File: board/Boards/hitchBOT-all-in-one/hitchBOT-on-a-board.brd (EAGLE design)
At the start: 160 x 100 mm, 7 parts

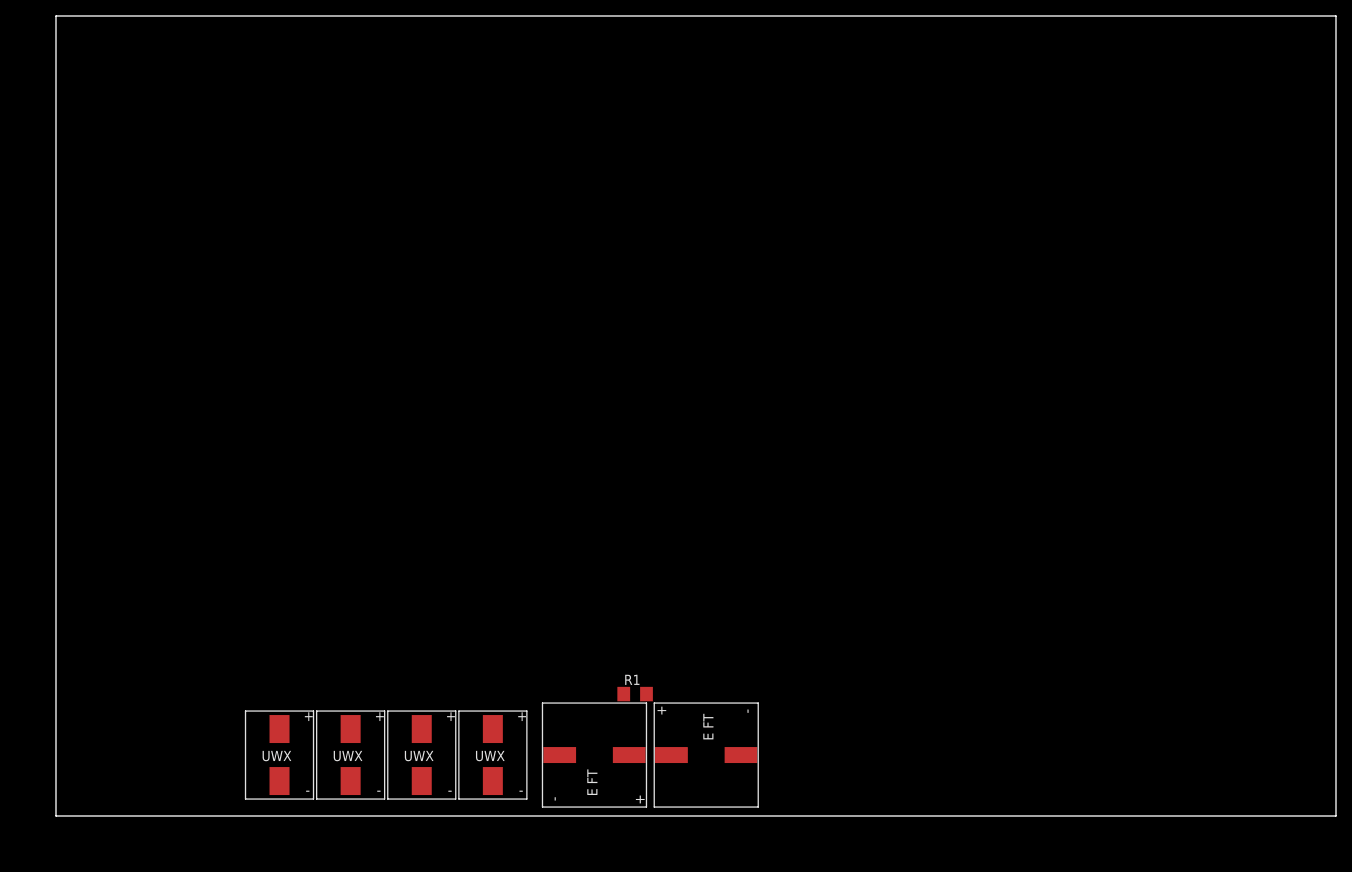
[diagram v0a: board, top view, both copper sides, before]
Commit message: updated board, now matches dimensions and layout of minibox board
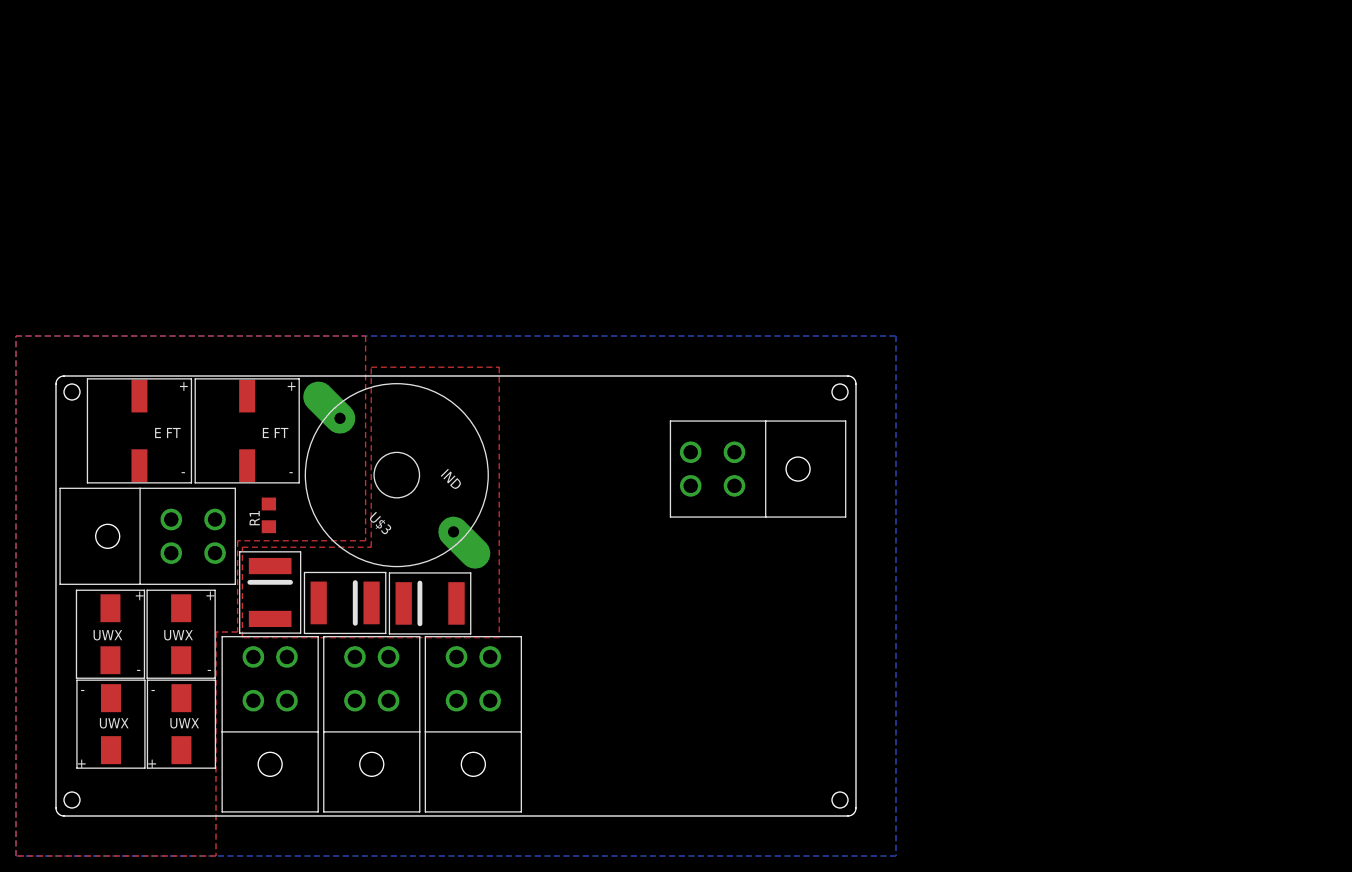
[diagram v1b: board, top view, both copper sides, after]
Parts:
- added U$10, U$11, U$4, U$5, U$6: 2X2-MOLEX, Molex:2X2MOLEX
- added U$3: INDUCTOR-M8365, macgrid:INDUCTOR-M8365
- added U$7, U$8, U$9: DO-214AB, macgrid:DO-214AB
- moved U$2 70.2 mm to (23.9, 48.1), turned to 0 degrees
- moved U$1 69.8 mm to (10.4, 48.1), turned to 0 degrees
- moved R1 50.9 mm to (26.6, 37.6), turned to 90 degrees
- moved C1 50.1 mm to (6.81, 22.7)
- moved C2 30.3 mm to (15.7, 11.5), turned to 180 degrees
- moved C4 30.2 mm to (6.87, 11.5), turned to 180 degrees
- moved C3 19.5 mm to (15.6, 22.7)
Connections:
- new net N$3: U$5.POWERL, U$5.POWERR, U$7.IN
- new net N$4: U$6.POWERL, U$6.POWERR, U$8.IN
- new net N$5: U$4.POWERL, U$4.POWERR, U$9.IN
- new net N$6: U$3.P$1, U$7.OUT, U$8.OUT, U$9.OUT
- net GND: now also U$10.GNDL, U$10.GNDR, U$11.GNDL, U$11.GNDR, U$4.GNDL, U$4.GNDR, U$5.GNDL, U$5.GNDR, U$6.GNDL, U$6.GNDR
- net N$1: now also U$10.POWERL, U$10.POWERR, U$3.P$2
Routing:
- added copper zone on layer 16, net GND
- added copper zone on layer 1, net N$1
- added copper zone on layer 1, net N$6
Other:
- board size 160 x 100 mm -> 100 x 55 mm
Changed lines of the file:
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@@
 <setting verticaltext="up"/>
 </settings>
-<grid distance="0.05" unitdist="inch" unit="inch" style="lines" multiple="1" display="no" altdistance="0.025" altunitdist="inch" altunit="inch"/>
+<grid distance="0.1" unitdist="mm" unit="mm" style="lines" multiple="1" display="no" altdistance="0.5" altunitdist="mm" altunit="mm"/>
 <layers>
 <layer number="1" name="Top" color="4" fill="1" visible="yes" active="yes"/>
@@
 <layer number="43" name="vRestrict" color="2" fill="10" visible="yes" active="yes"/>
 <layer number="44" name="Drills" color="7" fill="1" visible="no" active="yes"/>
-<layer number="45" name="Holes" color="7" fill="1" visible="no" active="yes"/>
+<layer number="45" name="Holes" color="7" fill="1" visible="yes" active="yes"/>
 <layer number="46" name="Milling" color="3" fill="1" visible="no" active="yes"/>
 <layer number="47" name="Measures" color="7" fill="1" visible="no" active="yes"/>
@@
 <board>
 <plain>
-<wire x1="0" y1="0" x2="160" y2="0" width="0" layer="20"/>
-<wire x1="160" y1="0" x2="160" y2="100" width="0" layer="20"/>
-<wire x1="160" y1="100" x2="0" y2="100" width="0" layer="20"/>
-<wire x1="0" y1="100" x2="0" y2="0" width="0" layer="20"/>
+<wire x1="0" y1="54" x2="0" y2="1" width="0" layer="20"/>
+<wire x1="0" y1="1" x2="1" y2="0" width="0" layer="20" curve="90"/>
+<wire x1="1" y1="0" x2="99" y2="0" width="0" layer="20"/>
+<wire x1="99" y1="0" x2="100" y2="1" width="0" layer="20" curve="90"/>
+<wire x1="100" y1="1" x2="100" y2="54" width="0" layer="20"/>
+<wire x1="100" y1="54" x2="99" y2="55" width="0" layer="20" curve="90"/>
+<wire x1="99" y1="55" x2="1" y2="55" width="0" layer="20"/>
+<wire x1="1" y1="55" x2="0" y2="54" width="0" layer="20" curve="90"/>
+<hole x="2" y="2" drill="2"/>
+<hole x="2" y="53" drill="2"/>
+<hole x="98" y="53" drill="2"/>
+<hole x="98" y="2" drill="2"/>
 </plain>
 <attributes>
@@
 </autorouter>
 <elements>
-<element name="C1" library="macgrid" package="SMD-CAP-8MM" value="SMD-CAP-NICHICON-8MM" x="54.61" y="7.62"/>
-<element name="C2" library="macgrid" package="SMD-CAP-8MM" value="SMD-CAP-NICHICON-8MM" x="45.72" y="7.62"/>
-<element name="C3" library="macgrid" package="SMD-CAP-8MM" value="SMD-CAP-NICHICON-8MM" x="27.94" y="7.62"/>
-<element name="C4" library="macgrid" package="SMD-CAP-8MM" value="SMD-CAP-NICHICON-8MM" x="36.83" y="7.62"/>
-<element name="U$1" library="macgrid" package="SMD-CAP-10MM" value="SMD-CAP-PANASONIC-E-FT-10MM" x="67.31" y="7.62" rot="R270"/>
-<element name="U$2" library="macgrid" package="SMD-CAP-10MM" value="SMD-CAP-PANASONIC-E-FT-10MM" x="81.28" y="7.62" rot="R90"/>
-<element name="R1" library="resistor" package="R1206" value="" x="72.39" y="15.24"/>
+<element name="C1" library="macgrid" package="SMD-CAP-8MM" value="SMD-CAP-NICHICON-8MM" x="6.81" y="22.72"/>
+<element name="C2" library="macgrid" package="SMD-CAP-8MM" value="SMD-CAP-NICHICON-8MM" x="15.68" y="11.48" rot="R180"/>
+<element name="C3" library="macgrid" package="SMD-CAP-8MM" value="SMD-CAP-NICHICON-8MM" x="15.64" y="22.72"/>
+<element name="C4" library="macgrid" package="SMD-CAP-8MM" value="SMD-CAP-NICHICON-8MM" x="6.87" y="11.48" rot="R180"/>
+<element name="U$1" library="macgrid" package="SMD-CAP-10MM" value="SMD-CAP-PANASONIC-E-FT-10MM" x="10.43" y="48.14"/>
+<element name="U$2" library="macgrid" package="SMD-CAP-10MM" value="SMD-CAP-PANASONIC-E-FT-10MM" x="23.9" y="48.14"/>
+<element name="R1" library="resistor" package="R1206" value="" x="26.61" y="37.58" rot="R90"/>
+<element name="U$3" library="macgrid" package="INDUCTOR-M8365" value="INDUCTOR-M8365" x="42.6" y="42.61" rot="R315"/>
+<element name="U$4" library="Molex" package="2X2MOLEX" value="2X2-MOLEX" x="39.47" y="16.51"/>
+<element name="U$5" library="Molex" package="2X2MOLEX" value="2X2-MOLEX" x="52.17" y="16.51"/>
+<element name="U$6" library="Molex" package="2X2MOLEX" value="2X2-MOLEX" x="26.77" y="16.51"/>
+<element name="U$7" library="macgrid" package="DO-214AB" value="DO-214AB" x="46.76" y="26.57" rot="R180"/>
+<element name="U$8" library="macgrid" package="DO-214AB" value="DO-214AB" x="26.77" y="27.94" rot="R90"/>
+<element name="U$9" library="macgrid" package="DO-214AB" value="DO-214AB" x="36.14" y="26.63"/>
+<element name="U$10" library="Molex" package="2X2MOLEX" value="2X2-MOLEX" x="16.51" y="34.96" rot="R270"/>
+<element name="U$11" library="Molex" package="2X2MOLEX" value="2X2-MOLEX" x="82.71" y="43.37" rot="R90"/>
 </elements>
 <signals>
@@
 <contactref element="C4" pad="P+"/>
 <contactref element="R1" pad="1"/>
-<wire x1="45.72" y1="10.87" x2="54.61" y2="10.87" width="0" layer="19" extent="1-1"/>
-<wire x1="36.83" y1="10.87" x2="45.72" y2="10.87" width="0" layer="19" extent="1-1"/>
-<wire x1="27.94" y1="10.87" x2="36.83" y2="10.87" width="0" layer="19" extent="1-1"/>
-<wire x1="70.968" y1="15.24" x2="27.94" y2="10.87" width="0" layer="19" extent="1-1"/>
+<contactref element="U$3" pad="P$2"/>
+<contactref element="U$10" pad="POWERL"/>
+<contactref element="U$10" pad="POWERR"/>
+<polygon width="0.4064" layer="1" isolate="0.4064">
+<vertex x="-5" y="-5"/>
+<vertex x="-5" y="60"/>
+<vertex x="38.7" y="60"/>
+<vertex x="38.7" y="34.4"/>
+<vertex x="22.7" y="34.4"/>
+<vertex x="22.7" y="23"/>
+<vertex x="20" y="23"/>
+<vertex x="20" y="-5"/>
+</polygon>
 </signal>
 <signal name="GND">
@@
 <contactref element="U$1" pad="P-"/>
 <contactref element="U$2" pad="P-"/>
-<wire x1="45.72" y1="4.37" x2="54.61" y2="4.37" width="0" layer="19" extent="1-1"/>
-<wire x1="36.83" y1="4.37" x2="45.72" y2="4.37" width="0" layer="19" extent="1-1"/>
-<wire x1="27.94" y1="4.37" x2="36.83" y2="4.37" width="0" layer="19" extent="1-1"/>
-<wire x1="62.96" y1="7.62" x2="27.94" y2="4.37" width="0" layer="19" extent="1-1"/>
-<wire x1="85.63" y1="7.62" x2="62.96" y2="7.62" width="0" layer="19" extent="1-1"/>
+<contactref element="U$5" pad="GNDL"/>
+<contactref element="U$5" pad="GNDR"/>
+<contactref element="U$6" pad="GNDL"/>
+<contactref element="U$6" pad="GNDR"/>
+<contactref element="U$4" pad="GNDL"/>
+<contactref element="U$4" pad="GNDR"/>
+<polygon width="0.4064" layer="16" isolate="0.3048">
+<vertex x="-5" y="-5"/>
+<vertex x="-5" y="60"/>
+<vertex x="105" y="60"/>
+<vertex x="105" y="-5"/>
+</polygon>
+<contactref element="U$10" pad="GNDL"/>
+<contactref element="U$10" pad="GNDR"/>
+<contactref element="U$11" pad="GNDL"/>
+<contactref element="U$11" pad="GNDR"/>
+<wire x1="14.41" y1="37.06" x2="23.9" y2="43.79" width="0" layer="19" extent="1-1"/>
+<wire x1="10.43" y1="43.79" x2="14.41" y2="37.06" width="0" layer="19" extent="1-1"/>
+<wire x1="15.68" y1="14.73" x2="24.67" y2="14.41" width="0" layer="19" extent="1-1"/>
+<wire x1="15.64" y1="19.47" x2="15.68" y2="14.73" width="0" layer="19" extent="1-1"/>
+<wire x1="6.81" y1="19.47" x2="15.64" y2="19.47" width="0" layer="19" extent="1-1"/>
+<wire x1="6.87" y1="14.73" x2="6.81" y2="19.47" width="0" layer="19" extent="1-1"/>
 </signal>
 <signal name="N$2">
@@
 <contactref element="U$1" pad="P+"/>
 <contactref element="U$2" pad="P+"/>
-<wire x1="76.93" y1="7.62" x2="73.812" y2="15.24" width="0" layer="19" extent="1-1"/>
-<wire x1="71.66" y1="7.62" x2="76.93" y2="7.62" width="0" layer="19" extent="1-1"/>
+<wire x1="10.43" y1="52.49" x2="23.9" y2="52.49" width="0" layer="19" extent="1-1"/>
+<wire x1="26.61" y1="39.002" x2="23.9" y2="52.49" width="0" layer="19" extent="1-1"/>
+</signal>
+<signal name="N$3">
+<contactref element="U$5" pad="POWERL"/>
+<contactref element="U$5" pad="POWERR"/>
+<contactref element="U$7" pad="IN"/>
+<wire x1="50.07" y1="19.88" x2="50.062" y2="26.57" width="0" layer="19" extent="1-1"/>
+<wire x1="54.27" y1="19.88" x2="50.07" y2="19.88" width="0" layer="19" extent="1-1"/>
+</signal>
+<signal name="N$4">
+<contactref element="U$6" pad="POWERL"/>
+<contactref element="U$6" pad="POWERR"/>
+<contactref element="U$8" pad="IN"/>
+<wire x1="28.87" y1="19.88" x2="26.77" y2="24.638" width="0" layer="19" extent="1-1"/>
+<wire x1="24.67" y1="19.88" x2="28.87" y2="19.88" width="0" layer="19" extent="1-1"/>
+</signal>
+<signal name="N$5">
+<contactref element="U$4" pad="POWERL"/>
+<contactref element="U$4" pad="POWERR"/>
+<contactref element="U$9" pad="IN"/>
+<wire x1="37.37" y1="19.88" x2="41.57" y2="19.88" width="0" layer="19" extent="1-1"/>
+<wire x1="32.838" y1="26.63" x2="37.37" y2="19.88" width="0" layer="19" extent="1-1"/>
+</signal>
+<signal name="N$6">
+<contactref element="U$9" pad="OUT"/>
+<contactref element="U$3" pad="P$1"/>
+<contactref element="U$8" pad="OUT"/>
+<contactref element="U$7" pad="OUT"/>
+<polygon width="0.4064" layer="1" isolate="0.4064">
+<vertex x="23.3" y="33.6"/>
+<vertex x="39.4" y="33.6"/>
+<vertex x="39.4" y="56.1"/>
+<vertex x="55.4" y="56.1"/>
+<vertex x="55.4" y="22.3"/>
+<vertex x="23.3" y="22.3"/>
+</polygon>
 </signal>
 </signals>
